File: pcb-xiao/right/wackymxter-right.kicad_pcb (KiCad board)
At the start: 2 copper layers, 162.7 x 127 mm, 81 parts, among them U1 xiao-ble, U2 74HC595

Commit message: Insane progresgress
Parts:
- BATTCONN1: moved to B.Cu
- moved BATTCONN1 2.05 mm to (60.0, 72.0), turned to 180 degrees
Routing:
- net row4: track 132.8 -> 246.6 mm, vias 0 -> 4
- net row3: track 180.0 -> 288.4 mm, vias 0 -> 2
- net row2: track 140.5 -> 240.0 mm, vias 0 -> 2
- net row1: track 140.5 -> 216.9 mm, vias 0 -> 1
- net B1: track 0.00 -> 72.8 mm
- net GND: track 96.4 -> 168.4 mm
- net ROTB: track 0.00 -> 66.2 mm, vias 0 -> 2
- net ROTA: track 0.00 -> 62.7 mm, vias 0 -> 2
- net row0: track 143.8 -> 201.1 mm
- net MOSI: track 0.00 -> 26.0 mm, vias 0 -> 1
- net SCK: track 0.00 -> 23.0 mm, vias 0 -> 1
- net col6: track 124.9 -> 146.3 mm
- net IO_CS: track 0.00 -> 15.2 mm, vias 0 -> 1
- net Net-(D18-A): track 2.55 -> 14.7 mm
- net Net-(D11-A): track 2.55 -> 14.7 mm
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- added copper zone on B.Cu, net GND
- added copper zone on F.Cu, net GND

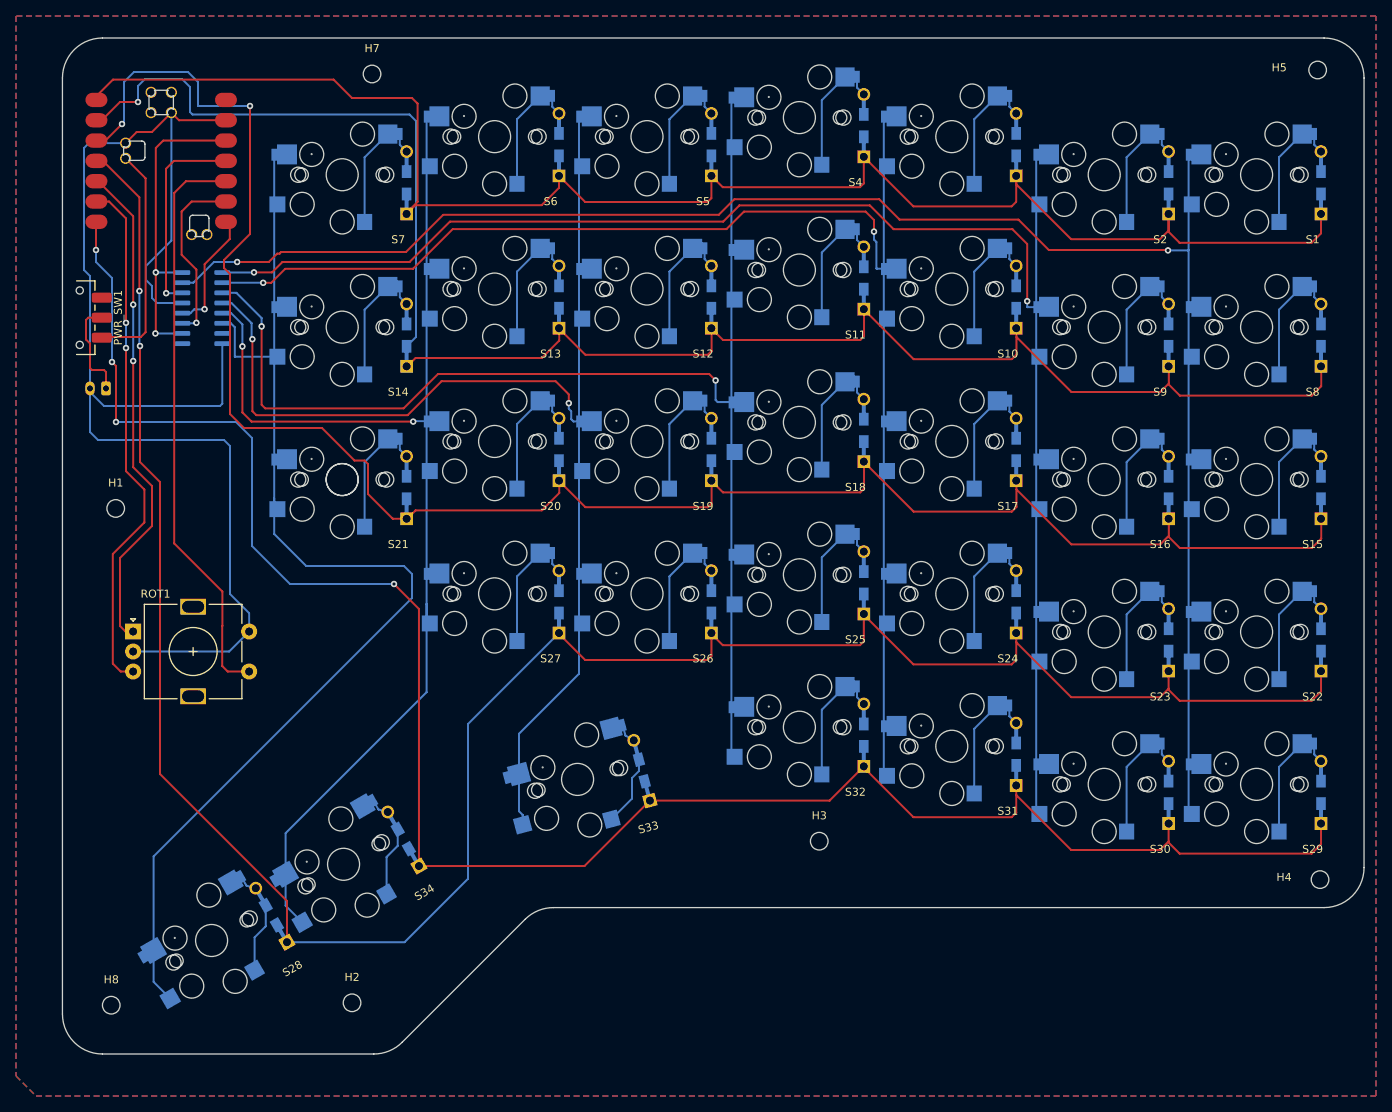
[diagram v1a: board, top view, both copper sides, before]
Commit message: Cooler cutout out and match schematics
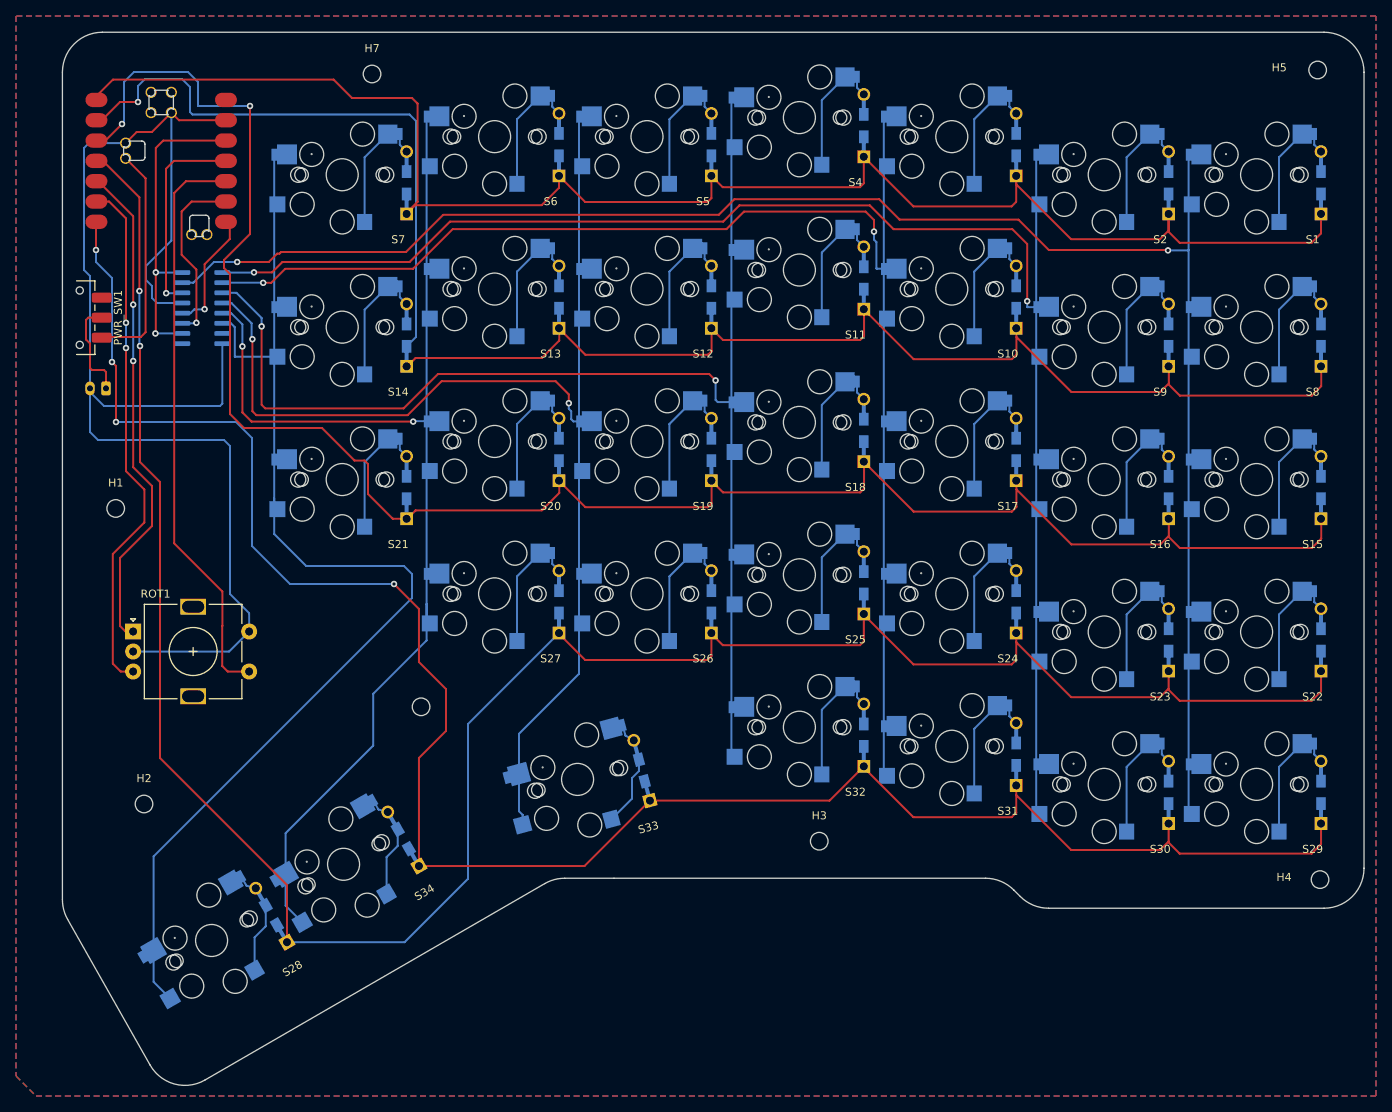
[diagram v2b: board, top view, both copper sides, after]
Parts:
- removed ?: , 
- removed H8: MountingHole, MountingHole:MountingHole_2.2mm_M2
- added H6: MountingHole, MountingHole:MountingHole_2.2mm_M2, B.Cu at (99.4, 111.8)
- U1: footprint mcu:xiao-ble-smd-cutout -> wackymxter:xiao-ble-smd-cutout
- moved H2 36.0 mm to (64.8, 123.9)
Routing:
- net row4: track 246.6 -> 249.4 mm
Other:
- board size 162.7 x 127 mm -> 162.7 x 131.6 mm
